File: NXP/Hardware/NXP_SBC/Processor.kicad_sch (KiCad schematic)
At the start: 1 part, among them U1 MCIMX6Y2DVM09AB

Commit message: Added some more to the DDR memory schematic
Upgraded the project to kicad 9.0
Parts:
- added C46, C47, C48, C49, C50, C51, C52, C53: 220nF, Capacitor_SMD:C_0603_1608Metric_Pad1.08x0.95mm_HandSolder, symbol Device:C_Small
- added C54: 10uF, Capacitor_SMD:C_0603_1608Metric_Pad1.08x0.95mm_HandSolder, symbol Device:C_Small
- added R45, R47, R48: 10k, Resistor_SMD:R_0603_1608Metric, symbol Device:R_Small
- added R46: 240R, 1%, Resistor_SMD:R_0603_1608Metric, symbol Device:R_Small
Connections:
- net DRAM_ODT1: now reaches U1.F1 (DRAM_ODT1)
- net DRAM_ADDR14: now reaches U1.G1 (DRAM_ADDR14)
- net DRAM_ADDR06: now reaches U1.G2 (DRAM_ADDR06)
- net at U1.G4 (DRAM_RESET): now also R45.2
- net +1V35: now reaches U1.G6 (NVCC_DRAM_1)
- net +1V35: now also U1.H6 (NVCC_DRAM_2), U1.J6 (NVCC_DRAM_3), U1.K6 (NVCC_DRAM_4), U1.L6 (NVCC_DRAM_5), U1.M6 (NVCC_DRAM_6), C48.1, C49.1, C50.1, C51.1, C52.1, C53.1, C54.1
- net DRAM_SDBA1: now reaches U1.H1 (DRAM_SDBA1)
- net DRAM_ADDR01: now reaches U1.H2 (DRAM_ADDR01)
- net DRAM_ADDR13: now reaches U1.H3 (DRAM_ADDR13)
- net DRAM_ADDR07: now reaches U1.H4 (DRAM_ADDR07)
- net DRAM_CS1_B: now reaches U1.H5 (DRAM_CS1_B)
- net DRAM_SDWE_B: now reaches U1.J1 (DRAM_SDWE_B)
- net DRAM_CAS_B: now reaches U1.J2 (DRAM_CAS_B)
- net at U1.J3 (DRAM_SDCKE1): now also R47.1
- net DRAM_ADDR08: now reaches U1.J4 (DRAM_ADDR08)
- net DRAM_ADDR02: now reaches U1.K1 (DRAM_ADDR02)
- net DRAM_SDBA2: now reaches U1.K2 (DRAM_SDBA2)
- net DRAM_ADDR11: now reaches U1.K3 (DRAM_ADDR11)
- net DRAM_ADDR04: now reaches U1.K4 (DRAM_ADDR04)
- net DRAM_ADDR15: now reaches U1.K5 (DRAM_ADDR15)
- net DRAM_ADDR05: now reaches U1.L1 (DRAM_ADDR05)
- net DRAM_ADDR09: now reaches U1.L2 (DRAM_ADDR09)
- net DRAM_ADDR12: now reaches U1.L4 (DRAM_ADDR12)
- net DRAM_ADDR00: now reaches U1.L5 (DRAM_ADDR00)
- net DRAM_SDBA0: now reaches U1.M1 (DRAM_SDBA0)
- net DRAM_ADDR03: now reaches U1.M2 (DRAM_ADDR03)
- net at U1.M3 (DRAM_SDCKE0): now also R48.1
- net DRAM_ADDR10: now reaches U1.M4 (DRAM_ADDR10)
- net DRAM_RAS_B: now reaches U1.M5 (DRAM_RAS_B)
- net DRAM_ODT0: now reaches U1.N1 (DRAM_ODT0)
- net DRAM_CS0_B: now reaches U1.N2 (DRAM_CS0_B)
- net at U1.N4 (DRAM_ZQPAD): now also R46.2
- net VDD_HIGH_CAP: now reaches U1.N6 (NVCC_DRAM_2P5)
- net VDD_HIGH_CAP: now also U1.R14 (VDD_HIGH_CAP_1), U1.R15 (VDD_HIGH_CAP_2), C47.1
- net DRAM_SDCLK0_P: now reaches U1.P1 (DRAM_SDCLK0_P)
- net DRAM_SDCLK0_N: now reaches U1.P2 (DRAM_SDCLK0_N)
- net DRAM_DATA13: now reaches U1.P3 (DRAM_DATA13)
- net DRAM_VREF: now reaches U1.P4 (DRAM_VREF)
- net DRAM_VREF: now also C46.1
- net DRAM_DATA12: now reaches U1.P5 (DRAM_DATA12)
- net DRAM_DATA15: now reaches U1.R1 (DRAM_DATA15)
- net DRAM_DATA14: now reaches U1.R2 (DRAM_DATA14)
- net DRAM_DATA11: now reaches U1.R4 (DRAM_DATA11)
- net DRAM_SDQS1_P: now reaches U1.T1 (DRAM_SDQS1_P)
- net DRAM_SDQS1_N: now reaches U1.T2 (DRAM_SDQS1_N)
- net DRAM_DQM1: now reaches U1.T3 (DRAM_DQM1)
- net DRAM_DATA0: now reaches U1.T4 (DRAM_DATA00)
- net DRAM_DATA6: now reaches U1.T5 (DRAM_DATA06)
- net DRAM_DATA2: now reaches U1.T6 (DRAM_DATA02)
- net DRAM_DATA5: now reaches U1.T8 (DRAM_DATA05)
- net DRAM_DATA8: now reaches U1.U2 (DRAM_DATA08)
- net DRAM_DATA9: now reaches U1.U3 (DRAM_DATA09)
- net DRAM_DATA7: now reaches U1.U4 (DRAM_DATA07)
- net DRAM_DATA10: now reaches U1.U5 (DRAM_DATA10)
- net DRAM_DATA1: now reaches U1.U6 (DRAM_DATA01)
- net DRAM_DATA3: now reaches U1.U7 (DRAM_DATA03)
- net DRAM_DATA4: now reaches U1.U8 (DRAM_DATA04)
- new net GND: C46.2, C47.2, C48.2, C49.2, C50.2, C51.2, C52.2, C53.2, C54.2, R45.1, R46.1, R47.2, R48.2
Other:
- moved on the sheet: U1C, U1D, U1E

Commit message: minor updates
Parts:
- added C55: 220nF, Capacitor_SMD:C_0603_1608Metric_Pad1.08x0.95mm_HandSolder, symbol Device:C_Small
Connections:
- net GND: now also C55.2
- net DRAM_SDQS0_P: now reaches U1.P6 (DRAM_SDQS0_P)
- net DRAM_SDSO_N: now reaches U1.P7 (DRAM_SDQS0_N)
- net DRAM_DQM0: now reaches U1.T7 (DRAM_DQM0)
- net LCD_DATA06: now reaches U1.A10 (LCD_DATA06)
- net LCD_DATA09: now reaches U1.A11 (LCD_DATA09)
- net LCD_DATA14: now reaches U1.A12 (LCD_DATA14)
- net LCD_DATA18: now reaches U1.A13 (LCD_DATA18)
- net LCD_DATA22: now reaches U1.A14 (LCD_DATA22)
- net LCD_CLK: now reaches U1.A8 (LCD_CLK)
- net LCD_DATA01: now reaches U1.A9 (LCD_DATA01)
- net LCD_DATA05: now reaches U1.B10 (LCD_DATA05)
- net LCD_DATA08: now reaches U1.B11 (LCD_DATA08)
- net LCD_DATA13: now reaches U1.B12 (LCD_DATA13)
- net LCD_DATA17: now reaches U1.B13 (LCD_DATA17)
- net LCD_DATA21: now reaches U1.B14 (LCD_DATA21)
- net LCD_DATA23: now reaches U1.B16 (LCD_DATA23)
- net LCD_ENABLE: now reaches U1.B8 (LCD_ENABLE)
- net LCD_DATA00: now reaches U1.B9 (LCD_DATA00)
- net LCD_DATA04: now reaches U1.C10 (LCD_DATA04)
- net LCD_DATA12: now reaches U1.C12 (LCD_DATA12)
- net LCD_DATA16: now reaches U1.C13 (LCD_DATA16)
- net LCD_DATA20: now reaches U1.C14 (LCD_DATA20)
- net LCD_VSYNC: now reaches U1.C9 (LCD_VSYNC)
- net LCD_DATA03: now reaches U1.D10 (LCD_DATA03)
- net LCD_DATA07: now reaches U1.D11 (LCD_DATA07)
- net LCD_DATA11: now reaches U1.D12 (LCD_DATA11)
- net LCD_DATA15: now reaches U1.D13 (LCD_DATA15)
- net LCD_DATA19: now reaches U1.D14 (LCD_DATA19)
- net LCD_HSYNC: now reaches U1.D9 (LCD_HSYNC)
- net LCD_DATA02: now reaches U1.E10 (LCD_DATA02)
- net LCD_DATA10: now reaches U1.E12 (LCD_DATA10)
- net DCDC_3V3: now reaches U1.E13 (NVCC_LCD)
- net DCDC_3V3: now also C55.1
- net LCD_RESET: now reaches U1.E9 (LCD_RESET)

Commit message: More additions to schematic
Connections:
- net GND: now also R47.1, R48.1; no longer R47.2, R48.2
- net uP_GPIO1_IO00: now reaches U1.K13 (GPIO1_IO00)
- net uP_ENET_MDIO: now reaches U1.K17 (GPIO1_IO06)
- net uP_GPIO1_IO02: now reaches U1.L14 (GPIO1_IO02)
- net uP_GPIO1_IO01: now reaches U1.L15 (GPIO1_IO01)
- net uP_ENET_MDC: now reaches U1.L16 (GPIO1_IO07)
- net uP_GPIO1_IO03: now reaches U1.L17 (GPIO1_IO03)
- net uP_GPIO1_IO09: now reaches U1.M15 (GPIO1_IO09)
- net uP_GPIO1_IO04: now reaches U1.M16 (GPIO1_IO04)
- net uP_GPIO1_IO05: now reaches U1.M17 (GPIO1_IO05)
- net uP_GPIO1_IO08: now reaches U1.N17 (GPIO1_IO08)
- net DRAM_SDKE1: now reaches U1.J3 (DRAM_SDCKE1)
- net DRAM_SDKE1: now also R48.2; no longer R47.1
- net DRAM_SDKE0: now reaches U1.M3 (DRAM_SDCKE0)
- net DRAM_SDKE0: now also R47.2; no longer R48.1
- net uP_ENET2_TX_DATA0: now reaches U1.A15 (ENET2_TX_DATA0)
- net uP_ENET2_TX_DATA1: now reaches U1.A16 (ENET2_TX_DATA1)
- net uP_ENET2_TX_EN: now reaches U1.B15 (ENET2_TX_EN)
- net uP_ENET2_RX_EN: now reaches U1.B17 (ENET2_RX_EN)
- net uP_ENET2_RX_DATA1: now reaches U1.C16 (ENET2_RX_DATA1)
- net uP_ENET2_RX_DATA0: now reaches U1.C17 (ENET2_RX_DATA0)
- net uP_ENET1_RX_ER: now reaches U1.D15 (ENET1_RX_ER)
- net uP_ENET2_RX_ER: now reaches U1.D16 (ENET2_RX_ER)
- net uP_ENET2_TX_CLK: now reaches U1.D17 (ENET2_TX_CLK)
- net uP_ENET1_TX_DATA1: now reaches U1.E14 (ENET1_TX_DATA1)
- net uP_ENET1_TX_DATA0: now reaches U1.E15 (ENET1_TX_DATA0)
- net uP_ENET1_RX_EN: now reaches U1.E16 (ENET1_RX_EN)
- net uP_ENET1_RX_DATA1: now reaches U1.E17 (ENET1_RX_DATA1)
- net uP_ENET1_TX_CLK: now reaches U1.F14 (ENET1_TX_CLK)
- net uP_ENET1_TX_EN: now reaches U1.F15 (ENET1_TX_EN)
- net uP_ENET1_RX_DATA0: now reaches U1.F16 (ENET1_RX_DATA0)
- net uP_UART5_TX_DATA: now reaches U1.F17 (UART5_TX_DATA)
- net uP_UART5_RX_DATA: now reaches U1.G13 (UART5_RX_DATA)
- net uP_UART3_RTS_B: now reaches U1.G14 (UART3_RTS_B)
- net uP_UART4_RX_DATA: now reaches U1.G16 (UART4_RX_DATA)
- net uP_UART4_TX_DATA: now reaches U1.G17 (UART4_TX_DATA)
- net uP_NVCC_UART: now reaches U1.H13 (NVCC_UART)
- net uP_UART2_RTS_B: now reaches U1.H14 (UART2_RTS_B)
- net uP_UART3_CTS_B: now reaches U1.H15 (UART3_CTS_B)
- net uP_UART3_RX_DATA: now reaches U1.H16 (UART3_RX_DATA)
- net uP_UART3_TX_DATA: now reaches U1.H17 (UART3_TX_DATA)
- net uP_UART1_RTS_B: now reaches U1.J14 (UART1_RTS_B)
- net uP_UART2_CTS_B: now reaches U1.J15 (UART2_CTS_B)
- net uP_UART2_RX_DATA: now reaches U1.J16 (UART2_RX_DATA)
- net uP_UART2_TX_DATA: now reaches U1.J17 (UART2_TX_DATA)
- net uP_UART1_TX_DATA: now reaches U1.K14 (UART1_TX_DATA)
- net uP_UART1_CTS_B: now reaches U1.K15 (UART1_CTS_B)
- net uP_UART1_RX_DATA: now reaches U1.K16 (UART1_RX_DATA)
- net uP_JTAG_TCK: now reaches U1.M14 (JTAG_TCK)
- net uP_JTAG_TRST_B: now reaches U1.N14 (JTAG_TRST_B)
- net uP_JTAG_TDO: now reaches U1.N15 (JTAG_TDO)
- net uP_JTAG_TDI: now reaches U1.N16 (JTAG_TDI)
- net uP_ENET1_nINT: now reaches U1.N8 (SNVS_TAMPER5)
- net uP_JTAG_TMS: now reaches U1.P14 (JTAG_TMS)
- net uP_JTAG_MOD: now reaches U1.P15 (JTAG_MOD)
- net uP_CCM_CLK1_N: now reaches U1.P16 (CCM_CLK1_N)
- net uP_CCM_CLK1_P: now reaches U1.P17 (CCM_CLK1_P)
- net uP_SD1_DATA3: now reaches U1.A2 (SD1_DATA3)
- net uP_SD1_DATA2: now reaches U1.B1 (SD1_DATA2)
- net uP_SD1_DATA1: now reaches U1.B2 (SD1_DATA1)
- net uP_SD1_DATA0: now reaches U1.B3 (SD1_DATA0)
- net uP_SD1_CLK: now reaches U1.C1 (SD1_CLK)
- net uP_SD1_CMD: now reaches U1.C2 (SD1_CMD)
- net DRAM_SDSO_N renamed DRAM_SDQSO_N
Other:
- moved on the sheet: R47, R48

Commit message: WIP
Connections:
- net DRAM_RESET: now reaches R45.2, U1.G4 (DRAM_RESET)
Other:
- moved on the sheet: R45, R46
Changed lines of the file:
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@@
 	)
 	(junction
-		(at 48.26 331.47)
+		(at 171.45 384.81)
 		(diameter 0)
 		(color 0 0 0 0)
 	)
 	(junction
-		(at 171.45 384.81)
+		(at 185.42 384.81)
 		(diameter 0)
 		(color 0 0 0 0)
 	)
 	(junction
-		(at 185.42 384.81)
+		(at 35.56 346.71)
 		(diameter 0)
 		(color 0 0 0 0)
@@
 	)
 	(junction
+		(at 35.56 325.12)
+		(diameter 0)
+		(color 0 0 0 0)
+	)
+	(junction
 		(at 198.12 384.81)
 		(diameter 0)
@@
 	(wire
 		(pts
+			(xy 30.48 325.12) (xy 35.56 325.12)
+		)
+		(stroke
+			(width 0)
+			(type default)
+		)
+	)
+	(wire
+		(pts
 			(xy 179.07 290.83) (xy 217.17 290.83)
 		)
@@
 	(wire
 		(pts
+			(xy 35.56 325.12) (xy 35.56 335.28)
+		)
+		(stroke
+			(width 0)
+			(type default)
+		)
+	)
+	(wire
+		(pts
 			(xy 210.82 349.25) (xy 198.12 349.25)
 		)
@@
 	(wire
 		(pts
+			(xy 35.56 325.12) (xy 100.33 325.12)
+		)
+		(stroke
+			(width 0)
+			(type default)
+		)
+	)
+	(wire
+		(pts
 			(xy 71.12 304.8) (xy 100.33 304.8)
 		)
@@
 	(wire
 		(pts
-			(xy 48.26 331.47) (xy 48.26 335.28)
+			(xy 35.56 340.36) (xy 35.56 346.71)
 		)
 		(stroke
@@
 	(wire
 		(pts
+			(xy 45.72 335.28) (xy 45.72 331.47)
+		)
+		(stroke
+			(width 0)
+			(type default)
+		)
+	)
+	(wire
+		(pts
 			(xy 680.72 166.37) (xy 641.35 166.37)
 		)
@@
 	(wire
 		(pts
-			(xy 71.12 256.54) (xy 100.33 256.54)
+			(xy 45.72 340.36) (xy 45.72 346.71)
 		)
 		(stroke
@@
 	(wire
 		(pts
-			(xy 179.07 265.43) (xy 217.17 265.43)
+			(xy 71.12 256.54) (xy 100.33 256.54)
 		)
 		(stroke
@@
 	(wire
 		(pts
-			(xy 449.58 455.93) (xy 467.36 455.93)
+			(xy 179.07 265.43) (xy 217.17 265.43)
 		)
 		(stroke
@@
 	(wire
 		(pts
-			(xy 295.91 121.92) (xy 312.42 121.92)
+			(xy 449.58 455.93) (xy 467.36 455.93)
 		)
 		(stroke
@@
 	(wire
 		(pts
-			(xy 680.72 158.75) (xy 641.35 158.75)
+			(xy 295.91 121.92) (xy 312.42 121.92)
 		)
 		(stroke
@@
 	(wire
 		(pts
-			(xy 171.45 373.38) (xy 171.45 375.92)
+			(xy 680.72 158.75) (xy 641.35 158.75)
 		)
 		(stroke
@@
 	(wire
 		(pts
-			(xy 680.72 179.07) (xy 641.35 179.07)
+			(xy 171.45 373.38) (xy 171.45 375.92)
 		)
 		(stroke
@@
 	(wire
 		(pts
-			(xy 377.19 387.35) (xy 377.19 391.16)
+			(xy 680.72 179.07) (xy 641.35 179.07)
 		)
 		(stroke
@@
 	(wire
 		(pts
-			(xy 92.71 325.12) (xy 100.33 325.12)
+			(xy 377.19 387.35) (xy 377.19 391.16)
 		)
 		(stroke
@@
 	(wire
 		(pts
+			(xy 45.72 346.71) (xy 35.56 346.71)
+		)
+		(stroke
+			(width 0)
+			(type default)
+		)
+	)
+	(wire
+		(pts
 			(xy 179.07 278.13) (xy 217.17 278.13)
 		)
@@
 	(wire
 		(pts
+			(xy 35.56 346.71) (xy 35.56 349.25)
+		)
+		(stroke
+			(width 0)
+			(type default)
+		)
+	)
+	(wire
+		(pts
 			(xy 179.07 254) (xy 217.17 254)
 		)
@@
 	(wire
 		(pts
-			(xy 48.26 325.12) (xy 48.26 331.47)
-		)
-		(stroke
-			(width 0)
-			(type default)
-		)
-	)
-	(wire
-		(pts
 			(xy 364.49 232.41) (xy 383.54 232.41)
 		)
@@
 	(wire
 		(pts
-			(xy 85.09 331.47) (xy 100.33 331.47)
+			(xy 45.72 331.47) (xy 100.33 331.47)
 		)
 		(stroke
@@
 	(wire
 		(pts
-			(xy 48.26 331.47) (xy 80.01 331.47)
-		)
-		(stroke
-			(width 0)
-			(type default)
-		)
-	)
-	(wire
-		(pts
 			(xy 295.91 149.86) (xy 312.42 149.86)
 		)
@@
 	(wire
 		(pts
-			(xy 87.63 325.12) (xy 48.26 325.12)
-		)
-		(stroke
-			(width 0)
-			(type default)
-		)
-	)
-	(wire
-		(pts
 			(xy 453.39 279.4) (xy 464.82 279.4)
 		)
@@
 		)
 	)
+	(hierarchical_label "DRAM_RESET"
+		(shape input)
+		(at 30.48 325.12 180)
+		(effects
+			(font
+				(size 1.27 1.27)
+			)
+			(justify right)
+		)
+	)
 	(hierarchical_label "DRAM_DATA15"
 		(shape input)
@@
 	(symbol
 		(lib_id "Device:R_Small")
-		(at 90.17 325.12 90)
+		(at 35.56 337.82 180)
 		(unit 1)
 		(exclude_from_sim no)
@@
 		(dnp no)
 		(property "Reference" "R45"
-			(at 90.17 323.088 90)
+			(at 33.528 337.82 90)
 			(effects
 				(font
@@
 		)
 		(property "Value" "10k"
-			(at 90.17 327.406 90)
+			(at 37.846 337.82 90)
 			(effects
 				(font
@@
 		)
 		(property "Footprint" "Resistor_SMD:R_0603_1608Metric"
-			(at 90.17 325.12 0)
+			(at 35.56 337.82 0)
 			(effects
 				(font
@@
 		)
 		(property "Datasheet" "~"
-			(at 90.17 325.12 0)
+			(at 35.56 337.82 0)
 			(effects
 				(font
@@
 		)
 		(property "Description" "Resistor, small symbol"
-			(at 90.17 325.12 0)
+			(at 35.56 337.82 0)
 			(effects
 				(font
@@
 	(symbol
 		(lib_id "Device:R_Small")
-		(at 82.55 331.47 90)
+		(at 45.72 337.82 180)
 		(unit 1)
 		(exclude_from_sim no)
@@
 		(dnp no)
 		(property "Reference" "R46"
-			(at 82.55 329.438 90)
+			(at 43.688 337.82 90)
 			(effects
 				(font
@@
 		)
 		(property "Value" "240R, 1%"
-			(at 82.55 333.502 90)
+			(at 47.752 337.82 90)
 			(effects
 				(font
@@
 		)
 		(property "Footprint" "Resistor_SMD:R_0603_1608Metric"
-			(at 82.55 331.47 0)
+			(at 45.72 337.82 0)
 			(effects
 				(font
@@
 		)
 		(property "Datasheet" "~"
-			(at 82.55 331.47 0)
+			(at 45.72 337.82 0)
 			(effects
 				(font
@@
 		)
 		(property "Description" "Resistor, small symbol"
-			(at 82.55 331.47 0)
+			(at 45.72 337.82 0)
 			(effects
 				(font
@@
 	(symbol
 		(lib_id "power:GND")
-		(at 48.26 335.28 0)
+		(at 35.56 349.25 0)
 		(unit 1)
 		(exclude_from_sim no)
@@
 		(fields_autoplaced yes)
 		(property "Reference" "#PWR062"
-			(at 48.26 341.63 0)
+			(at 35.56 355.6 0)
 			(effects
 				(font
@@
 		)
 		(property "Value" "GND"
-			(at 48.26 340.36 0)
+			(at 35.56 354.33 0)
 			(effects
 				(font
@@
 		)
 		(property "Footprint" ""
-			(at 48.26 335.28 0)
+			(at 35.56 349.25 0)
 			(effects
 				(font
@@
 		)
 		(property "Datasheet" ""
-			(at 48.26 335.28 0)
+			(at 35.56 349.25 0)
 			(effects
 				(font
@@
 		)
 		(property "Description" "Power symbol creates a global label with name \"GND\" , ground"
-			(at 48.26 335.28 0)
+			(at 35.56 349.25 0)
 			(effects
 				(font

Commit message: More updates to schematic
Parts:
- added R75, R76: 10k, Resistor_SMD:R_0603_1608Metric, symbol Device:R_Small
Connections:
- net uP_UART4_RX_DATA renamed uP_I2C_SDA
- net uP_I2C_SDA: now also R76.1
- net uP_UART4_TX_DATA renamed uP_I2C_SCL
- net uP_I2C_SCL: now also R75.1
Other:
- note added: "DOUBLE CHECK PULL UP VOLTAGE"

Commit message: WIP
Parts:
- added R77, R78, R79, R80: 0R, Resistor_SMD:R_0603_1608Metric, symbol Device:R_Small
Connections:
- net uP_ENET1_nINT: now also R78.1; no longer U1.N8 (SNVS_TAMPER5)
- net at U1.N10 (SNVS_TAMPER7): now also R80.2
- net at U1.N9 (SNVS_TAMPER8): now also R79.2
- net at U1.R6 (SNVS_TAMPER9): now also R77.2
- net uP_USB_OTG1_DN: now reaches U1.T15 (USB_OTG1_DN)
- net uP_USB_OTG1_DP: now reaches U1.U15 (USB_OTG1_DP)
- new net: R78.2, U1.N8 (SNVS_TAMPER5)
- new net uP_LCD_DISP: R77.1
- new net uP_TS_INT: R79.1
- new net uP_TS_RESET: R80.1

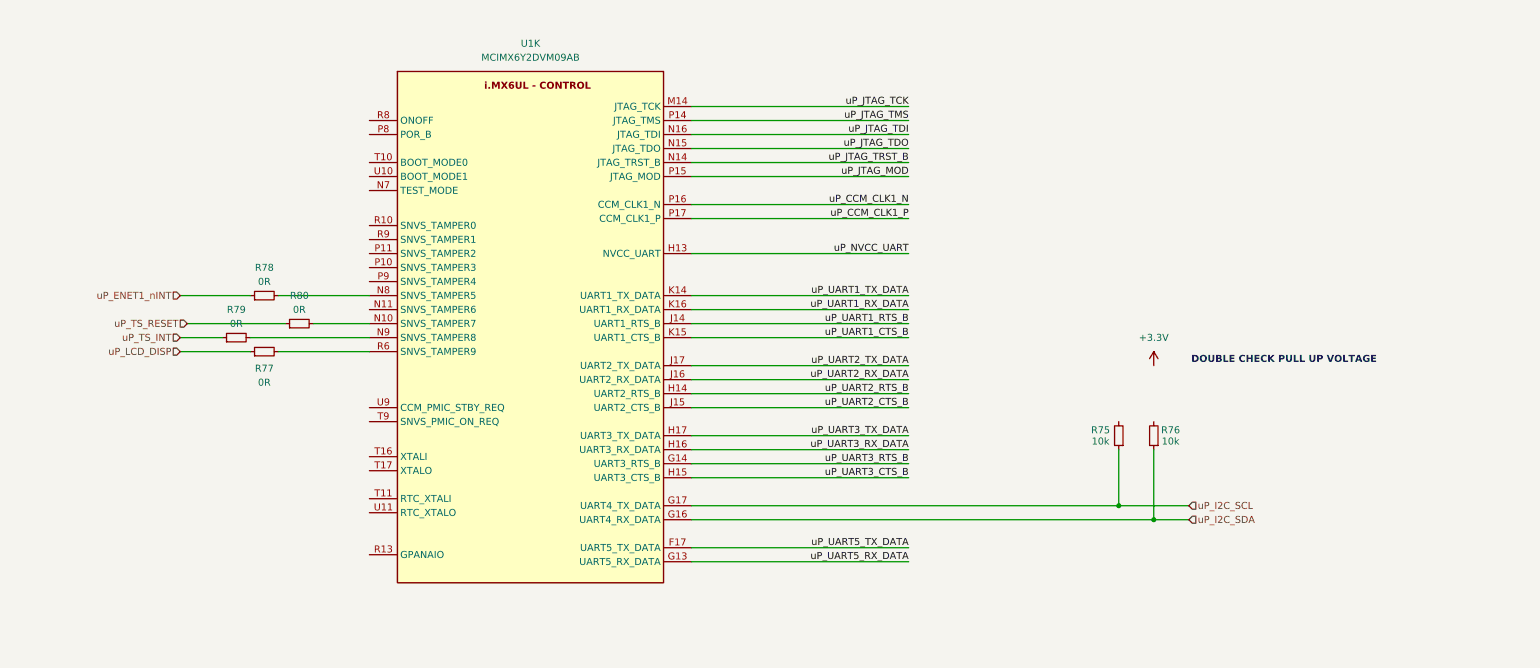
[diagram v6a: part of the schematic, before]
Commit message: Finished audio section
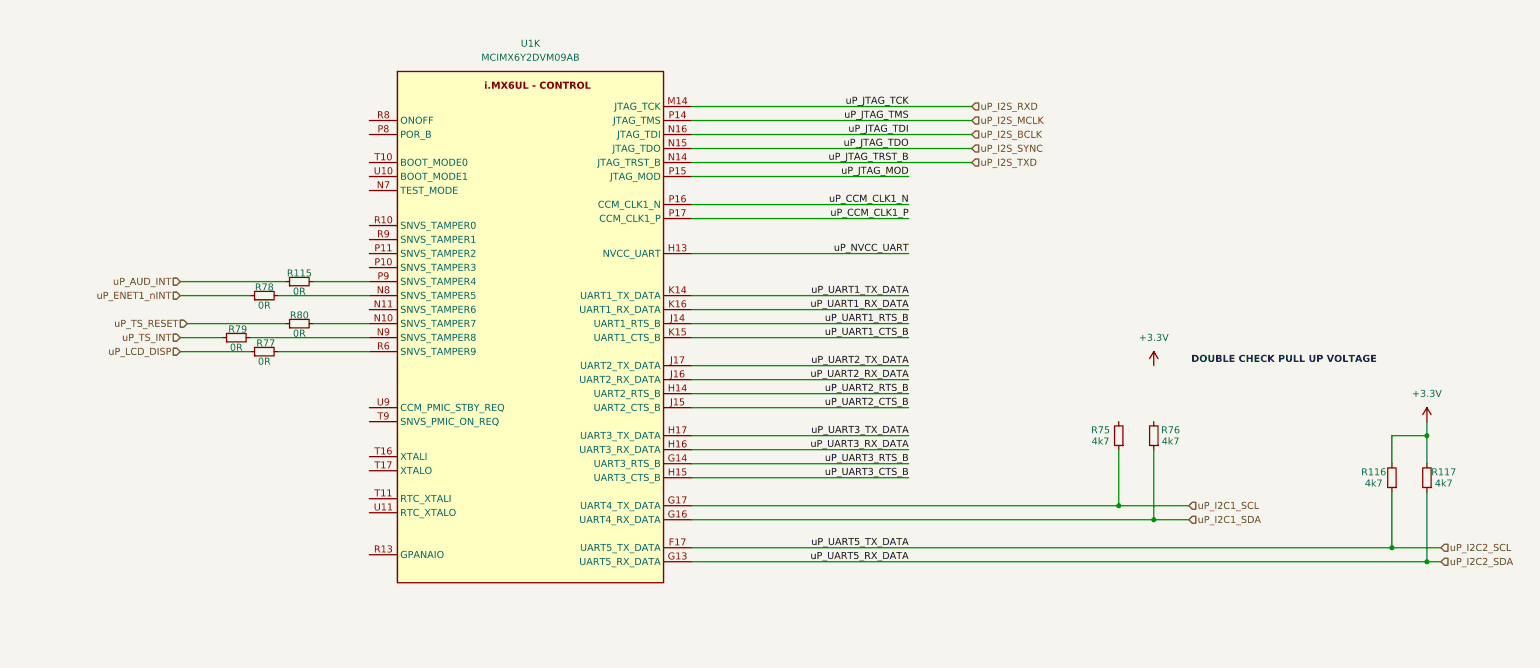
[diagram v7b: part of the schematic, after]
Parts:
- added R115: 0R, Resistor_SMD:R_0603_1608Metric, symbol Device:R_Small
- added R116, R117: 4k7, Resistor_SMD:R_0603_1608Metric, symbol Device:R_Small
- R75, R76: value 10k -> 4k7
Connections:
- net +3.3V: now also R116.2, R117.2
- net at U1.P9 (SNVS_TAMPER4): now also R115.2
- net uP_I2C_SCL renamed uP_I2C1_SCL
- net uP_I2C_SDA renamed uP_I2C1_SDA
- net uP_JTAG_TCK renamed uP_I2S_RXD
- net uP_JTAG_TDI renamed uP_I2S_BCLK
- net uP_JTAG_TDO renamed uP_I2S_SYNC
- net uP_JTAG_TMS renamed uP_I2S_MCLK
- net uP_JTAG_TRST_B renamed uP_I2S_TXD
- net uP_UART5_RX_DATA renamed uP_I2C2_SDA
- net uP_I2C2_SDA: now also R117.1
- net uP_UART5_TX_DATA renamed uP_I2C2_SCL
- net uP_I2C2_SCL: now also R116.1
- new net uP_AUD_INT: R115.1

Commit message: Updates to radio connections
Also used the pin configurator tool to better understand pin mapping of the imx processor
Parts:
- added C107, C108: 220nF, Capacitor_SMD:C_0603_1608Metric_Pad1.08x0.95mm_HandSolder, symbol Device:C_Small
- added R138, R139, R140, R141, R142, R143, R144: 0R, Resistor_SMD:R_0603_1608Metric, symbol Device:R_Small
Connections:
- net uP_NVCC_UART is gone; now on net DCDC_3V3: U1.H13 (NVCC_UART)
- net +3.3V: now also R75.2, R76.2
- net DCDC_3V3: now also C107.1
- net GND: now also C107.2
- net at U1.D1 (CSI_DATA07): now also R144.1
- net at U1.D2 (CSI_DATA06): now also R143.1
- net at U1.D3 (CSI_DATA05): now also R142.1
- net at U1.D4 (CSI_DATA04): now also R141.1
- net at U1.E1 (CSI_DATA03): now also R140.1
- net at U1.E2 (CSI_DATA02): now also R139.1
- net at U1.E3 (CSI_DATA01): now also R138.1
- net +1V8_RADIO: now reaches U1.F4 (NVCC_CSI)
- net uP_GPIO4_IO9: now reaches U1.A5 (NAND_DATA07)
- net uP_GPIO4_IO8: now reaches U1.A6 (NAND_DATA06)
- net RADIO_SD_DATA2: now reaches U1.A7 (NAND_DATA02)
- net uP_GPIO4_IO7: now reaches U1.B6 (NAND_DATA05)
- net RADIO_SD_DATA1: now reaches U1.B7 (NAND_DATA01)
- net uP_GPIO4_IO6: now reaches U1.C6 (NAND_DATA04)
- net RADIO_SD_CMD: now reaches U1.C8 (NAND_WE_B)
- net RADIO_SD_DATA3: now reaches U1.D6 (NAND_DATA03)
- net RADIO_SD_DATA0: now reaches U1.D7 (NAND_DATA00)
- net RADIO_SD_CLK: now reaches U1.D8 (NAND_RE_B)
- new net uP_SAI1_MCLK: R138.2
- new net uP_SAI1_RX_BCLK: R140.2
- new net uP_SAI1_RX_DATA: R143.2
- new net uP_SAI1_RX_SYNC: R139.2
- new net uP_SAI1_TX_BCLK: R142.2
- new net uP_SAI1_TX_DATA: R144.2
- new net uP_SAI1_TX_SYNC: R141.2
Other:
- note added: "RTS/CTS can be swapped in IO_MUX on chip"
- note added: "USED FOR RADIO RESETS/WAKE"
